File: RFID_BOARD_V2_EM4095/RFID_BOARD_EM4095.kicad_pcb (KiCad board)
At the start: 2 copper layers, 25 x 30 mm, 31 parts, among them J1 CONN_01X05, U1 EM4095

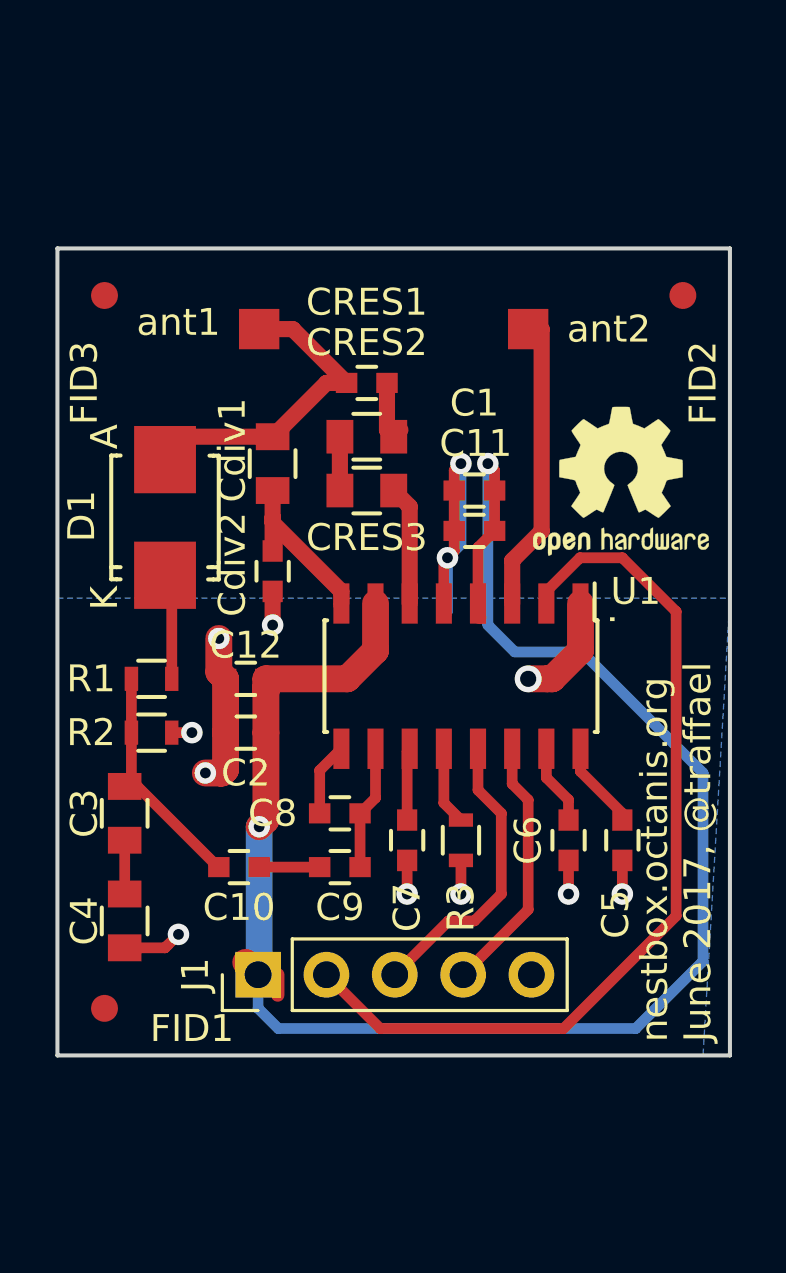
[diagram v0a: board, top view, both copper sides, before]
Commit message: second PCB for EM4095 and created fabrication files of main board and corrected holes locations
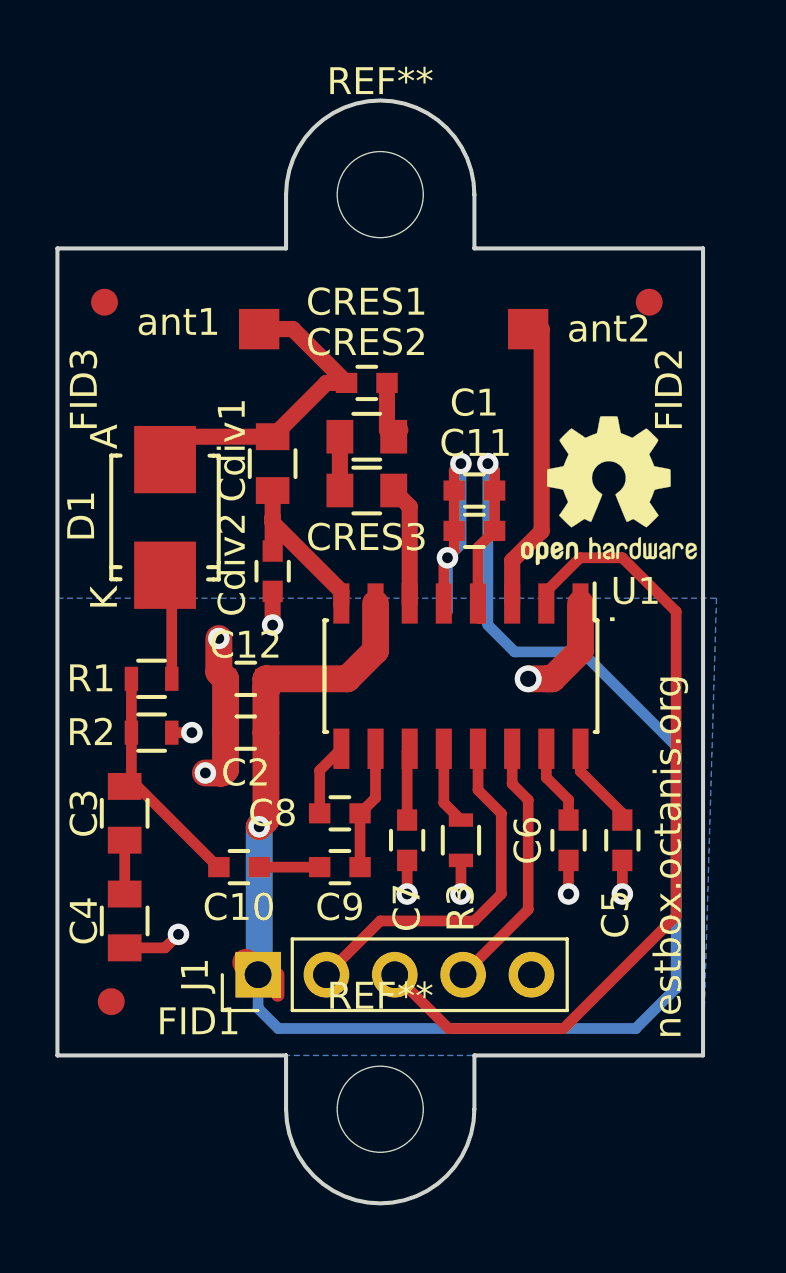
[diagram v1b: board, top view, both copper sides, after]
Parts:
- added REF**: MountingHole_3.2mm_M3, Mounting_Holes:MountingHole_3.2mm_M3, F.Cu at (157.0, 94.5)
- added REF**: MountingHole_3.2mm_M3, Mounting_Holes:MountingHole_3.2mm_M3, F.Cu at (157.0, 128.5)
- moved FID2 1.27 mm to (167.0, 98.5)
- moved REF*** 0.57 mm to (165.5, 105.5)
- moved FID1 0.35 mm to (147.0, 124.5)
- moved FID3 0.25 mm to (146.8, 98.5)
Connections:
- J1 pad 2: /rdyclk -> /demod_out
- J1 pad 3: /demod_out -> /rdyclk
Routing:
- net /demod_out: track 11.0 -> 13.5 mm
- net /rdyclk: track 33.5 -> 31.0 mm
- net /RFID_VDD: track 67.5 -> 66.7 mm
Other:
- board size 25 x 30 mm -> 24 x 41 mm
- board text added: "G S C D V"
- board text added: "nestbox.octanis.org"
- board text removed: "G S D C V"
- board text removed: "nestbox.octanis.org June 2017, @traffael"

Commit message: TAPEOUT second batch nestbox main + EM pcb. added pull-ups, corrected pmos of load cell, WIFI AND SDCARD ENABLE PMOS ARE STILL WRONGLY ORIENTED
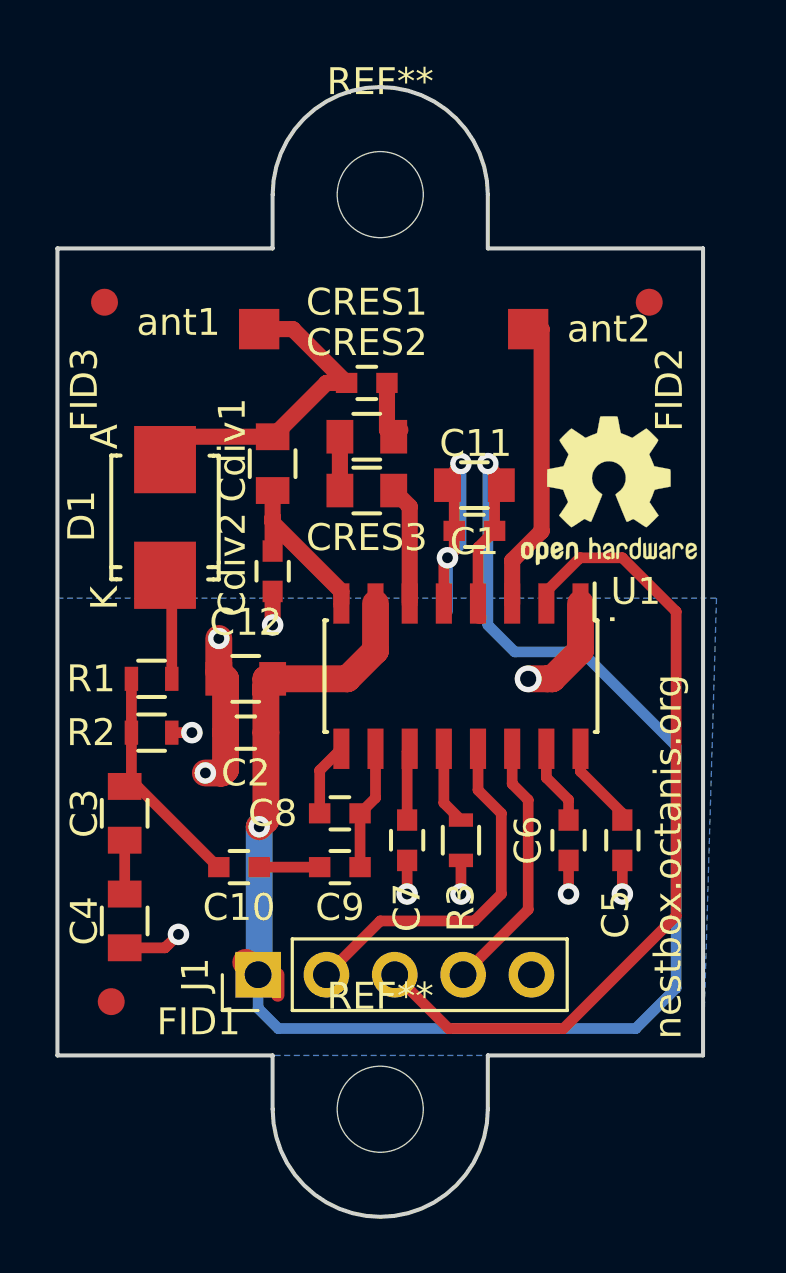
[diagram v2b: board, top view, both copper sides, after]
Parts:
- C1, C12: footprint Capacitors_SMD:C_0603 -> Capacitors_SMD:C_0805
- C5: value 10n - 22n max -> 10n (22n max)
- C8: value DNP -> DNP or 100n
- Cdiv2: value C -> 1.5n
- moved C1 0.20 mm to (160.5, 105.3)
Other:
- board size 24 x 41 mm -> 24 x 42 mm
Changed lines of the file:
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@@
   (general
     (links 46)
-    (no_connects 4)
+    (no_connects 2)
     (area 129.811904 89.325 183.938096 139.200001)
     (thickness 1.6)
@@
     (pad_to_mask_clearance 0.2)
     (aux_axis_origin 0 0)
-    (grid_origin 145 132)
+    (grid_origin 145 126.5)
     (visible_elements FFFF7F3F)
     (pcbplotparams
@@
       (effects (font (size 1 1) (thickness 0.15)))
     )
-    (fp_text value "10n - 22n max" (at 0 1.9 90) (layer F.Fab)
+    (fp_text value "10n  (22n max)" (at 0 1.9 90) (layer F.Fab)
       (effects (font (size 1 1) (thickness 0.15)))
     )
@@
       (effects (font (size 1 1) (thickness 0.15)))
     )
-    (fp_text value DNP (at 0 1.9) (layer F.Fab)
+    (fp_text value "DNP or 100n" (at 0 1.9) (layer F.Fab)
       (effects (font (size 1 1) (thickness 0.15)))
     )
@@
       (effects (font (size 1 1) (thickness 0.15)))
     )
-    (fp_text value C (at 0 1.9 90) (layer F.Fab)
+    (fp_text value 1.5n (at 0 1.9 90) (layer F.Fab)
       (effects (font (size 1 1) (thickness 0.15)))
     )
@@
     (pad 2 smd rect (at 0.75 0 180) (size 0.8 0.75) (layers F.Cu F.Paste F.Mask)
       (net 1 GND))
-    (model Capacitors_SMD.3dshapes/C_0603.wrl
-      (at (xyz 0 0 0))
-      (scale (xyz 1 1 1))
-      (rotate (xyz 0 0 0))
-    )
-  )
-  (module Capacitors_SMD:C_0603 (layer F.Cu)
-    (at 160.5 105.5 180)
-    (descr "Capacitor SMD 0603, reflow soldering, AVX (see smccp.pdf)")
-    (tags "capacitor 0603")
-    (attr smd)
-    (fp_text reference C1 (at 0 3.25 180) (layer F.SilkS)
-      (effects (font (size 1 1) (thickness 0.15)))
-    )
-    (fp_text value 10u (at 0 1.9 180) (layer F.Fab)
-      (effects (font (size 1 1) (thickness 0.15)))
-    )
-    (fp_line (start -0.8 0.4) (end -0.8 -0.4) (layer F.Fab) (width 0.15))
-    (fp_line (start 0.8 0.4) (end -0.8 0.4) (layer F.Fab) (width 0.15))
-    (fp_line (start 0.8 -0.4) (end 0.8 0.4) (layer F.Fab) (width 0.15))
-    (fp_line (start -0.8 -0.4) (end 0.8 -0.4) (layer F.Fab) (width 0.15))
-    (fp_line (start -1.45 -0.75) (end 1.45 -0.75) (layer F.CrtYd) (width 0.05))
-    (fp_line (start -1.45 0.75) (end 1.45 0.75) (layer F.CrtYd) (width 0.05))
-    (fp_line (start -1.45 -0.75) (end -1.45 0.75) (layer F.CrtYd) (width 0.05))
-    (fp_line (start 1.45 -0.75) (end 1.45 0.75) (layer F.CrtYd) (width 0.05))
-    (fp_line (start -0.35 -0.6) (end 0.35 -0.6) (layer F.SilkS) (width 0.15))
-    (fp_line (start 0.35 0.6) (end -0.35 0.6) (layer F.SilkS) (width 0.15))
-    (pad 1 smd rect (at -0.75 0 180) (size 0.8 0.75) (layers F.Cu F.Paste F.Mask)
-      (net 2 /RFID_VDD))
-    (pad 2 smd rect (at 0.75 0 180) (size 0.8 0.75) (layers F.Cu F.Paste F.Mask)
-      (net 1 GND))
-    (model Capacitors_SMD.3dshapes/C_0603.wrl
-      (at (xyz 0 0 0))
-      (scale (xyz 1 1 1))
-      (rotate (xyz 0 0 0))
-    )
-  )
-  (module Capacitors_SMD:C_0603 (layer F.Cu)
-    (at 152 112.5)
-    (descr "Capacitor SMD 0603, reflow soldering, AVX (see smccp.pdf)")
-    (tags "capacitor 0603")
-    (attr smd)
-    (fp_text reference C12 (at 0 -1.25) (layer F.SilkS)
-      (effects (font (size 1 1) (thickness 0.15)))
-    )
-    (fp_text value 10u (at 0 1.9) (layer F.Fab)
-      (effects (font (size 1 1) (thickness 0.15)))
-    )
-    (fp_line (start -0.8 0.4) (end -0.8 -0.4) (layer F.Fab) (width 0.15))
-    (fp_line (start 0.8 0.4) (end -0.8 0.4) (layer F.Fab) (width 0.15))
-    (fp_line (start 0.8 -0.4) (end 0.8 0.4) (layer F.Fab) (width 0.15))
-    (fp_line (start -0.8 -0.4) (end 0.8 -0.4) (layer F.Fab) (width 0.15))
-    (fp_line (start -1.45 -0.75) (end 1.45 -0.75) (layer F.CrtYd) (width 0.05))
-    (fp_line (start -1.45 0.75) (end 1.45 0.75) (layer F.CrtYd) (width 0.05))
-    (fp_line (start -1.45 -0.75) (end -1.45 0.75) (layer F.CrtYd) (width 0.05))
-    (fp_line (start 1.45 -0.75) (end 1.45 0.75) (layer F.CrtYd) (width 0.05))
-    (fp_line (start -0.35 -0.6) (end 0.35 -0.6) (layer F.SilkS) (width 0.15))
-    (fp_line (start 0.35 0.6) (end -0.35 0.6) (layer F.SilkS) (width 0.15))
-    (pad 1 smd rect (at -0.75 0) (size 0.8 0.75) (layers F.Cu F.Paste F.Mask)
-      (net 1 GND))
-    (pad 2 smd rect (at 0.75 0) (size 0.8 0.75) (layers F.Cu F.Paste F.Mask)
-      (net 2 /RFID_VDD))
     (model Capacitors_SMD.3dshapes/C_0603.wrl
       (at (xyz 0 0 0))
@@
     (pad 1 np_thru_hole circle (at 0 0) (size 3.2 3.2) (drill 3.2) (layers *.Cu *.Mask))
   )
-  (gr_line (start 160.5 94.5) (end 160.5 96.5) (layer Edge.Cuts) (width 0.15))
-  (gr_arc (start 157 94.5) (end 153.5 94.5) (angle 180) (layer Edge.Cuts) (width 0.15))
-  (gr_line (start 153.5 94.5) (end 153.5 96.5) (layer Edge.Cuts) (width 0.15))
-  (gr_arc (start 157 128.5) (end 160.5 128.5) (angle 180) (layer Edge.Cuts) (width 0.15))
-  (gr_line (start 169 96.5) (end 160.5 96.5) (layer Edge.Cuts) (width 0.15))
-  (gr_line (start 160.5 126.5) (end 169 126.5) (layer Edge.Cuts) (width 0.15))
-  (gr_line (start 160.5 128.5) (end 160.5 126.5) (layer Edge.Cuts) (width 0.15))
-  (gr_line (start 153.5 128.5) (end 153.5 126.5) (layer Edge.Cuts) (width 0.15))
+  (module Capacitors_SMD:C_0805 (layer F.Cu)
+    (at 160.5 105.3 180)
+    (descr "Capacitor SMD 0805, reflow soldering, AVX (see smccp.pdf)")
+    (tags "capacitor 0805")
+    (attr smd)
+    (fp_text reference C1 (at 0 -2.1 180) (layer F.SilkS)
+      (effects (font (size 1 1) (thickness 0.15)))
+    )
+    (fp_text value 10u (at 0 2.1 180) (layer F.Fab)
+      (effects (font (size 1 1) (thickness 0.15)))
+    )
+    (fp_line (start -1 0.625) (end -1 -0.625) (layer F.Fab) (width 0.15))
+    (fp_line (start 1 0.625) (end -1 0.625) (layer F.Fab) (width 0.15))
+    (fp_line (start 1 -0.625) (end 1 0.625) (layer F.Fab) (width 0.15))
+    (fp_line (start -1 -0.625) (end 1 -0.625) (layer F.Fab) (width 0.15))
+    (fp_line (start -1.8 -1) (end 1.8 -1) (layer F.CrtYd) (width 0.05))
+    (fp_line (start -1.8 1) (end 1.8 1) (layer F.CrtYd) (width 0.05))
+    (fp_line (start -1.8 -1) (end -1.8 1) (layer F.CrtYd) (width 0.05))
+    (fp_line (start 1.8 -1) (end 1.8 1) (layer F.CrtYd) (width 0.05))
+    (fp_line (start 0.5 -0.85) (end -0.5 -0.85) (layer F.SilkS) (width 0.15))
+    (fp_line (start -0.5 0.85) (end 0.5 0.85) (layer F.SilkS) (width 0.15))
+    (pad 1 smd rect (at -1 0 180) (size 1 1.25) (layers F.Cu F.Paste F.Mask)
+      (net 2 /RFID_VDD))
+    (pad 2 smd rect (at 1 0 180) (size 1 1.25) (layers F.Cu F.Paste F.Mask)
+      (net 1 GND))
+    (model Capacitors_SMD.3dshapes/C_0805.wrl
+      (at (xyz 0 0 0))
+      (scale (xyz 1 1 1))
+      (rotate (xyz 0 0 0))
+    )
+  )
+  (module Capacitors_SMD:C_0805 (layer F.Cu)
+    (at 152 112.5)
+    (descr "Capacitor SMD 0805, reflow soldering, AVX (see smccp.pdf)")
+    (tags "capacitor 0805")
+    (attr smd)
+    (fp_text reference C12 (at 0 -2.1) (layer F.SilkS)
+      (effects (font (size 1 1) (thickness 0.15)))
+    )
+    (fp_text value 10u (at 0 2.1) (layer F.Fab)
+      (effects (font (size 1 1) (thickness 0.15)))
+    )
+    (fp_line (start -1 0.625) (end -1 -0.625) (layer F.Fab) (width 0.15))
+    (fp_line (start 1 0.625) (end -1 0.625) (layer F.Fab) (width 0.15))
+    (fp_line (start 1 -0.625) (end 1 0.625) (layer F.Fab) (width 0.15))
+    (fp_line (start -1 -0.625) (end 1 -0.625) (layer F.Fab) (width 0.15))
+    (fp_line (start -1.8 -1) (end 1.8 -1) (layer F.CrtYd) (width 0.05))
+    (fp_line (start -1.8 1) (end 1.8 1) (layer F.CrtYd) (width 0.05))
+    (fp_line (start -1.8 -1) (end -1.8 1) (layer F.CrtYd) (width 0.05))
+    (fp_line (start 1.8 -1) (end 1.8 1) (layer F.CrtYd) (width 0.05))
+    (fp_line (start 0.5 -0.85) (end -0.5 -0.85) (layer F.SilkS) (width 0.15))
+    (fp_line (start -0.5 0.85) (end 0.5 0.85) (layer F.SilkS) (width 0.15))
+    (pad 1 smd rect (at -1 0) (size 1 1.25) (layers F.Cu F.Paste F.Mask)
+      (net 1 GND))
+    (pad 2 smd rect (at 1 0) (size 1 1.25) (layers F.Cu F.Paste F.Mask)
+      (net 2 /RFID_VDD))
+    (model Capacitors_SMD.3dshapes/C_0805.wrl
+      (at (xyz 0 0 0))
+      (scale (xyz 1 1 1))
+      (rotate (xyz 0 0 0))
+    )
+  )
+  (gr_line (start 161 94.5) (end 161 96.5) (layer Edge.Cuts) (width 0.15))
+  (gr_arc (start 157 94.5) (end 153 94.5) (angle 180) (layer Edge.Cuts) (width 0.15))
+  (gr_line (start 153 94.5) (end 153 96.5) (layer Edge.Cuts) (width 0.15))
+  (gr_arc (start 157 128.5) (end 161 128.5) (angle 180) (layer Edge.Cuts) (width 0.15))
+  (gr_line (start 169 96.5) (end 161 96.5) (layer Edge.Cuts) (width 0.15))
+  (gr_line (start 161 126.5) (end 169 126.5) (layer Edge.Cuts) (width 0.15))
+  (gr_line (start 161 128.5) (end 161 126.5) (layer Edge.Cuts) (width 0.15))
+  (gr_line (start 153 128.5) (end 153 126.5) (layer Edge.Cuts) (width 0.15))
   (dimension 12 (width 0.3) (layer F.Fab)
     (gr_text "12.000 mm" (at 151 137.85) (layer F.Fab)
@@
   )
   (gr_line (start 145 96.5) (end 145 126.5) (layer Edge.Cuts) (width 0.15))
-  (gr_line (start 153.5 96.5) (end 145 96.5) (layer Edge.Cuts) (width 0.15))
+  (gr_line (start 153 96.5) (end 145 96.5) (layer Edge.Cuts) (width 0.15))
   (gr_line (start 169 126.5) (end 169 96.5) (layer Edge.Cuts) (width 0.15))
-  (gr_line (start 145 126.5) (end 153.5 126.5) (layer Edge.Cuts) (width 0.15))
+  (gr_line (start 145 126.5) (end 153 126.5) (layer Edge.Cuts) (width 0.15))
   (gr_text "RFID Reader (EM4095)" (at 167.5 99.5) (layer B.SilkS)
     (effects (font (size 1.2 1.2) (thickness 0.25)) (justify left mirror))
